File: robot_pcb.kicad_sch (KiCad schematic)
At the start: 112 parts, among them J1 Raspberry_Pi_2_3, J10 Servo_TrayRelease, J14 Motor FR, J16 19V Output, J17 Programmer, J2 Power_Bypass, J23 Motor BR, J25 ConductClaw, J26 Motor BL, J27 TOF_Front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

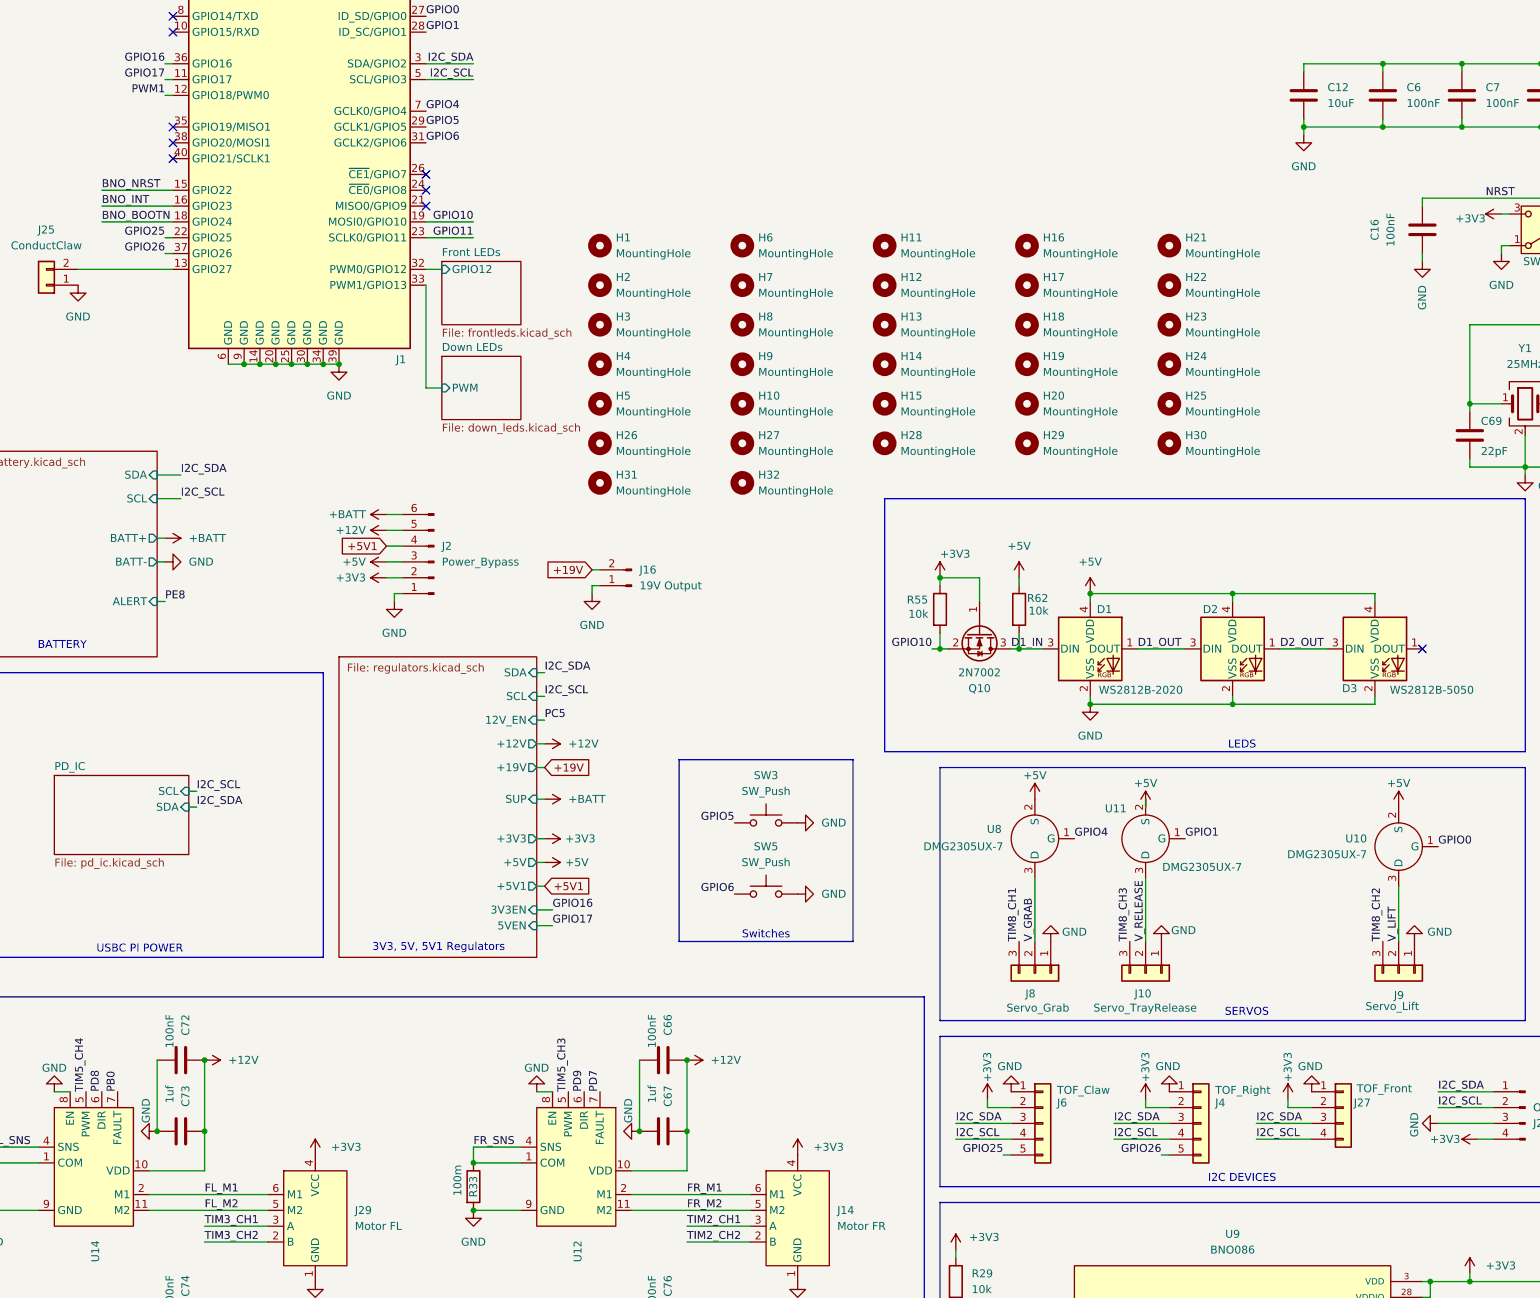
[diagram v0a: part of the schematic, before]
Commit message: 6 pin tof sensors
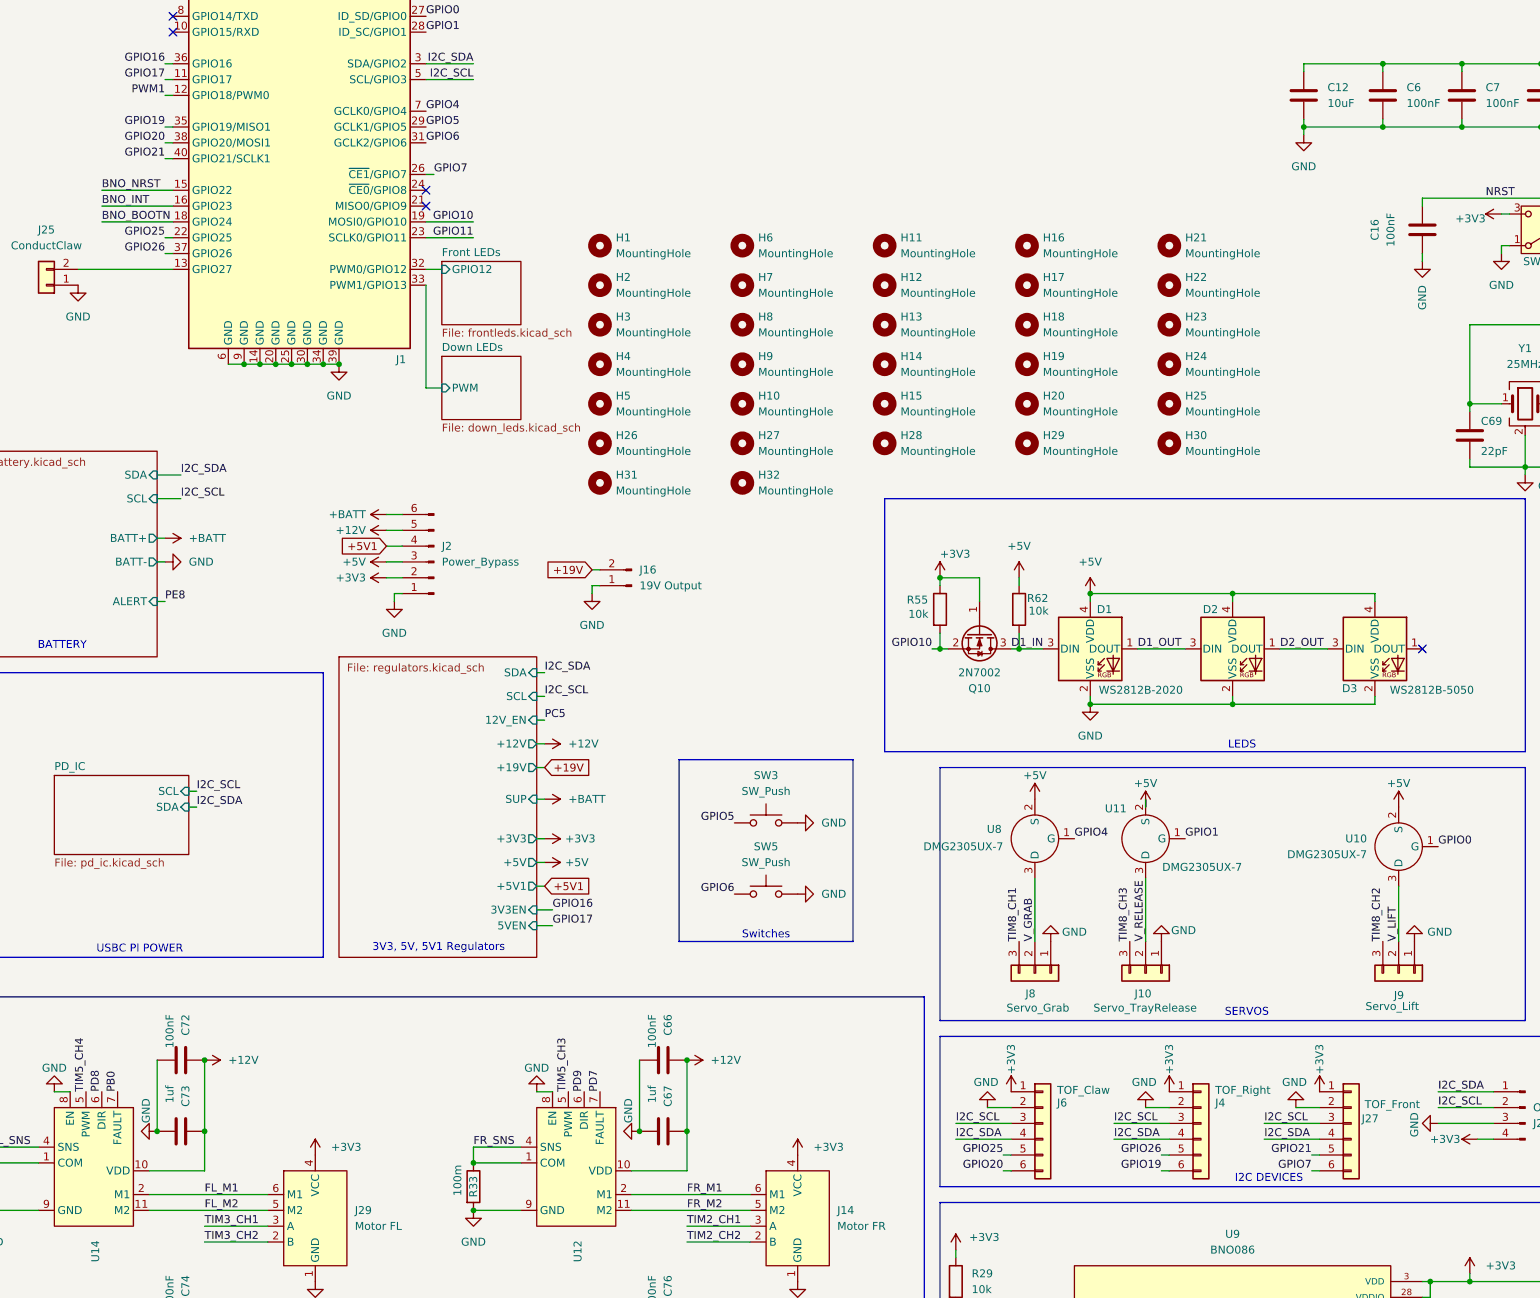
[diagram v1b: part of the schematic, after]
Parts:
- J10, J8, J9: LCSC (none) -> C158004
- J14, J23, J26, J29: LCSC (none) -> C157920
- J17, J7: LCSC (none) -> C52016392
- J25: LCSC (none) -> C5251182
- J27: footprint Connector_JST:JST_PH_B4B-PH-K_1x04_P2.00mm_Vertical -> Connector_JST:JST_PH_B6B-PH-K_1x06_P2.00mm_Vertical; symbol Connector_Generic:Conn_01x04 -> Connector_Generic:Conn_01x06
- J4, J6: footprint Connector_JST:JST_PH_B5B-PH-K_1x05_P2.00mm_Vertical -> Connector_JST:JST_PH_B6B-PH-K_1x06_P2.00mm_Vertical; symbol Connector_Generic:Conn_01x05 -> Connector_Generic:Conn_01x06
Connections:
- net +3V3: now also J27.1 (Pin_1), J4.1 (Pin_1), J6.1 (Pin_1); no longer J27.2 (Pin_2), J4.2 (Pin_2), J6.2 (Pin_2)
- net GND: now also J27.2 (Pin_2), J4.2 (Pin_2), J6.2 (Pin_2); no longer J27.1 (Pin_1), J4.1 (Pin_1), J6.1 (Pin_1)
- net I2C_SCL: now also J27.3 (Pin_3), J4.3 (Pin_3), J6.3 (Pin_3); no longer J27.4 (Pin_4), J4.4 (Pin_4), J6.4 (Pin_4)
- net I2C_SDA: now also J27.4 (Pin_4), J4.4 (Pin_4), J6.4 (Pin_4); no longer J27.3 (Pin_3), J4.3 (Pin_3), J6.3 (Pin_3)
- net GPIO7: now reaches J1.26 (~{CE1}/GPIO7)
- net GPIO7: now also J27.6 (Pin_6)
- net GPIO19: now reaches J1.35 (GPIO19/MISO1)
- net GPIO19: now also J4.6 (Pin_6)
- net GPIO20: now reaches J1.38 (GPIO20/MOSI1)
- net GPIO20: now also J6.6 (Pin_6)
- net GPIO21: now reaches J1.40 (GPIO21/SCLK1)
- net GPIO21: now also J27.5 (Pin_5)
- no-connect marks 66 -> 62

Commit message: yes
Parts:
- J16: LCSC (none) -> C158007
- J2: LCSC (none) -> C52016393
- J27, J4, J6: LCSC (none) -> C495261
- J28: LCSC (none) -> C2718488
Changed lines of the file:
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@@
 			)
 		)
-		(property "LCSC" ""
+		(property "LCSC" "C495261"
 			(at 237.49 208.28 0)
 			(effects
@@
 			)
 		)
+		(property "LCSC" "C495261"
+			(at 213.36 208.28 0)
+			(effects
+				(font
+					(size 1.27 1.27)
+				)
+				(hide yes)
+			)
+		)
 		(pin "3"
 		)
@@
 			)
 		)
-		(property "LCSC" ""
+		(property "LCSC" "C2718488"
 			(at 265.43 205.74 0)
 			(effects
@@
 			)
 		)
+		(property "LCSC" "C158007"
+			(at 121.92 121.92 0)
+			(effects
+				(font
+					(size 1.27 1.27)
+				)
+				(hide yes)
+			)
+		)
 		(pin "2"
 		)
@@
 			)
 		)
+		(property "LCSC" "C52016393"
+			(at 90.17 118.11 0)
+			(effects
+				(font
+					(size 1.27 1.27)
+				)
+				(hide yes)
+			)
+		)
 		(pin "5"
 		)
@@
 			(at 187.96 208.28 0)
 			(effects
+				(font
+					(size 1.27 1.27)
+				)
+				(hide yes)
+			)
+		)
+		(property "LCSC" "C495261"
+			(at 187.96 208.28 0)
+			(effects

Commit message: more lcsc
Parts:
- J1: LCSC (none) -> C50980
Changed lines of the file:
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@@
 			)
 		)
-		(property "LCSC" ""
+		(property "LCSC" "C50980"
 			(at 68.58 53.34 0)
 			(effects

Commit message: ALL LCSC PARTS DONE
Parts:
- M1: LCSC (none) -> C240840
- U12, U14, U15, U16: LCSC (none) -> C194048
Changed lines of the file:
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@@
 			)
 		)
+		(property "LCSC" "C194048"
+			(at 121.92 251.46 0)
+			(effects
+				(font
+					(size 1.27 1.27)
+				)
+				(hide yes)
+			)
+		)
 		(pin "11"
 		)
@@
 			)
 		)
+		(property "LCSC" "C240840"
+			(at 339.09 240.03 0)
+			(effects
+				(font
+					(size 1.27 1.27)
+				)
+				(hide yes)
+			)
+		)
 		(pin "3"
 		)
@@
 			)
 		)
+		(property "LCSC" "C194048"
+			(at 44.45 251.46 0)
+			(effects
+				(font
+					(size 1.27 1.27)
+				)
+				(hide yes)
+			)
+		)
 		(pin "11"
 		)
@@
 			)
 		)
+		(property "LCSC" "C194048"
+			(at 121.92 209.55 0)
+			(effects
+				(font
+					(size 1.27 1.27)
+				)
+				(hide yes)
+			)
+		)
 		(pin "11"
 		)
@@
 			(at 44.45 209.55 0)
 			(effects
+				(font
+					(size 1.27 1.27)
+				)
+				(hide yes)
+			)
+		)
+		(property "LCSC" "C194048"
+			(at 44.45 209.55 0)
+			(effects

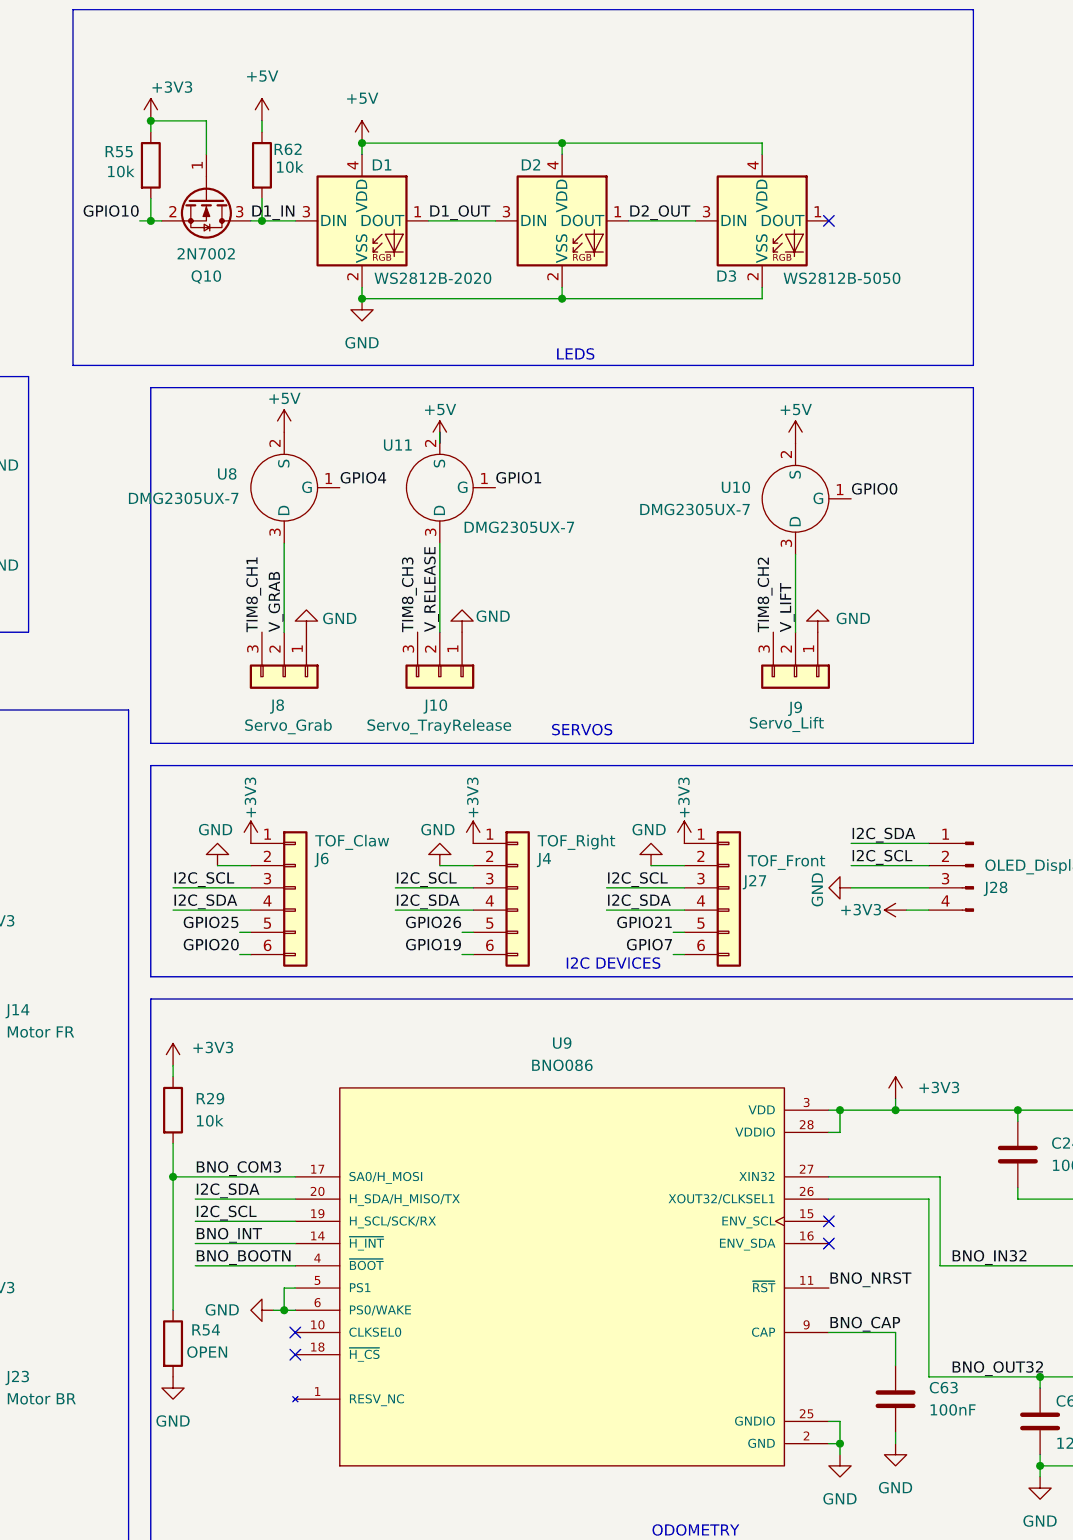
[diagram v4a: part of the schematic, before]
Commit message: Fixed errors with open resistors and led
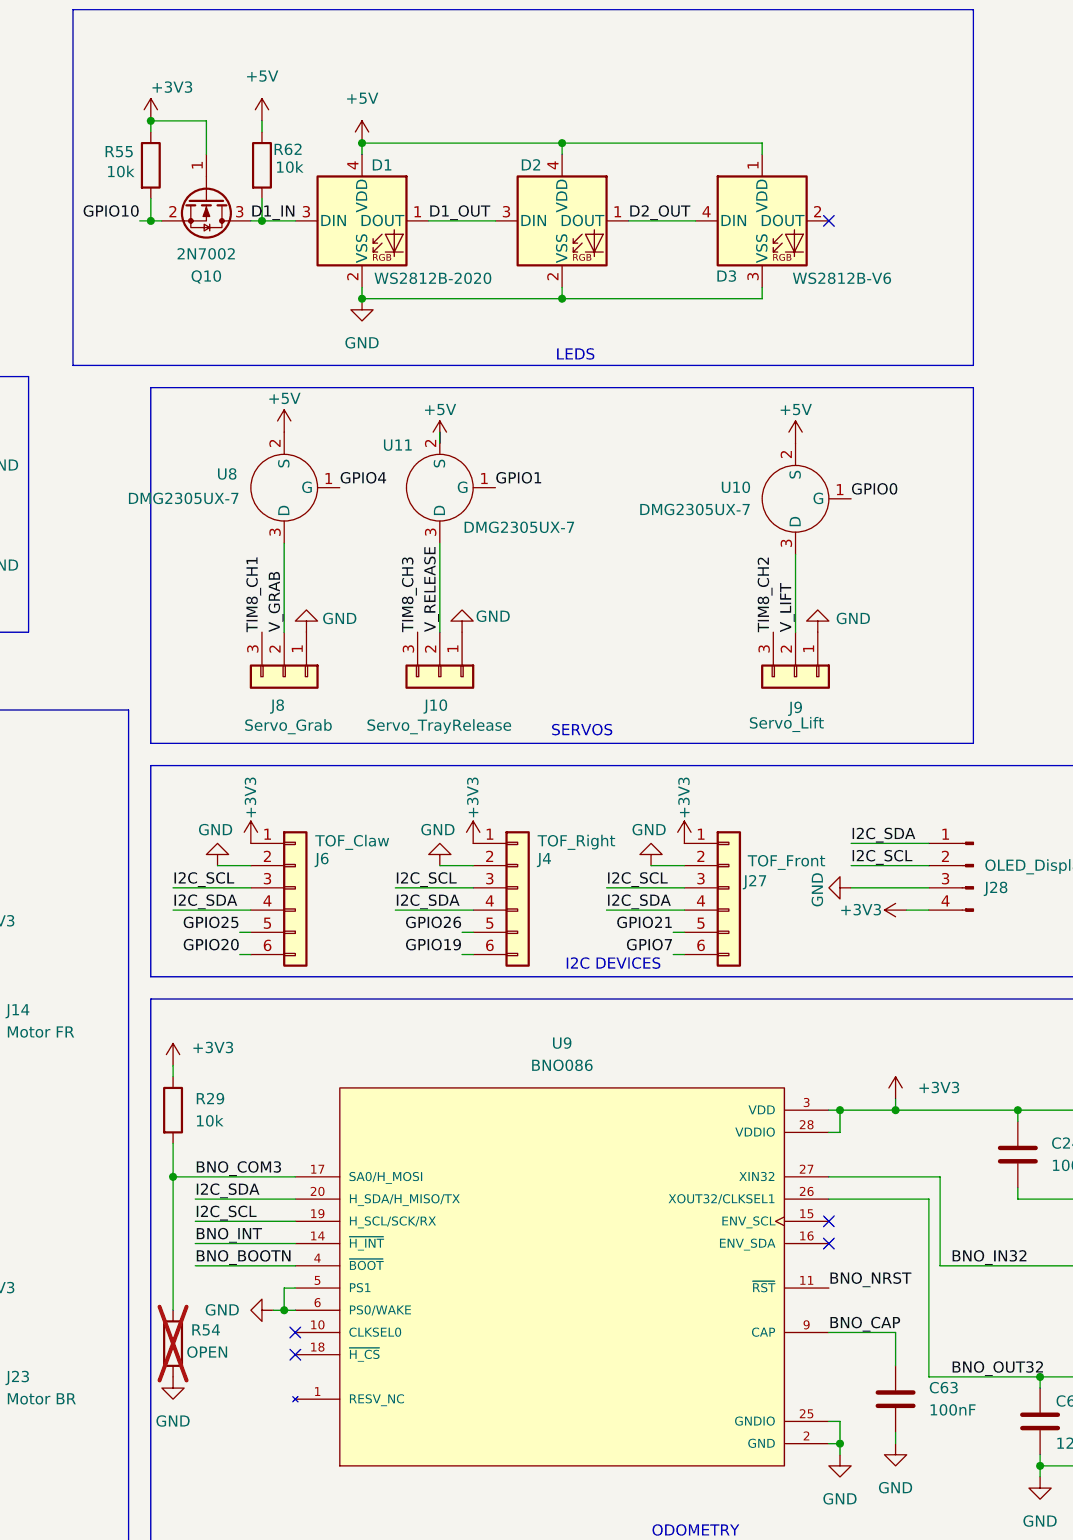
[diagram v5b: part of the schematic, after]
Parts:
- D3: value WS2812B-5050 -> WS2812B-V6; symbol LED:WS2812B-2020 -> Dry_Lettuce:WS2812B-5050; LCSC C114586 -> C52917433
- R54: now not fitted; now left out of the parts list
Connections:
- net +5V: now also D3.1 (VDD); no longer D3.4 (VDD)
- net D2_OUT: now also D3.4 (DIN); no longer D3.3 (DIN)
- net GND: now also D3.3 (VSS); no longer D3.2 (VSS)
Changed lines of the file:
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@@
 	)
 	(symbol
-		(lib_id "LED:WS2812B-2020")
+		(lib_id "Dry_Lettuce:WS2812B-5050")
 		(at 241.3 132.08 0)
 		(unit 1)
@@
 			)
 		)
-		(property "Value" "WS2812B-5050"
+		(property "Value" "WS2812B-V6"
 			(at 250.444 138.684 0)
 			(effects
@@
 			)
 		)
-		(property "Datasheet" "https://cdn-shop.adafruit.com/product-files/4684/4684_WS2812B-2020_V1.3_EN.pdf"
+		(property "Datasheet" "https://www.lcsc.com/datasheet/C52917433.pdf"
 			(at 243.84 141.605 0)
 			(effects
@@
 			)
 		)
-		(property "Description" "RGB LED with integrated controller, 2.0 x 2.0 mm, 12 mA"
-			(at 241.3 132.08 0)
-			(effects
-				(font
-					(size 1.27 1.27)
-				)
-				(hide yes)
-			)
-		)
-		(property "LCSC" "C114586"
+		(property "Description" "RGB LED with integrated controller, 5.0 x 5.0 mm, 12 mA"
+			(at 271.272 145.034 0)
+			(effects
+				(font
+					(size 1.27 1.27)
+				)
+				(hide yes)
+			)
+		)
+		(property "LCSC" "C52917433"
 			(at 241.3 132.08 0)
 			(effects
@@
 		(unit 1)
 		(exclude_from_sim no)
-		(in_bom yes)
-		(on_board yes)
-		(dnp no)
+		(in_bom no)
+		(on_board yes)
+		(dnp yes)
 		(property "Reference" "R54"
 			(at 176.022 258.826 0)

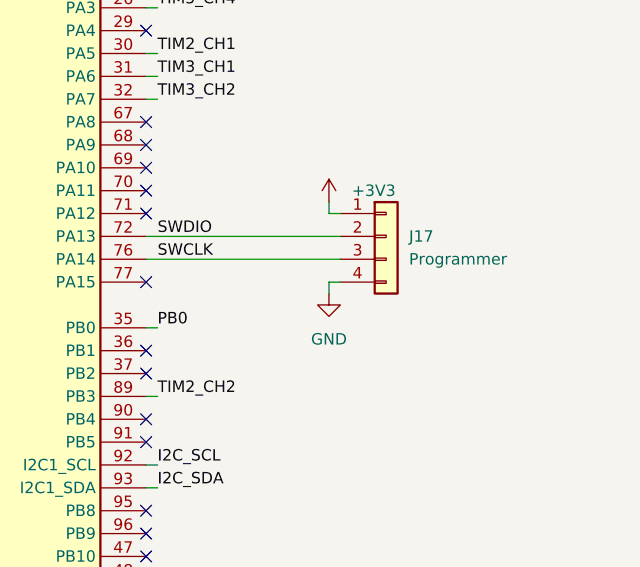
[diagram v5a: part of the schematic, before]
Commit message: added reset pin to stm32 debug output
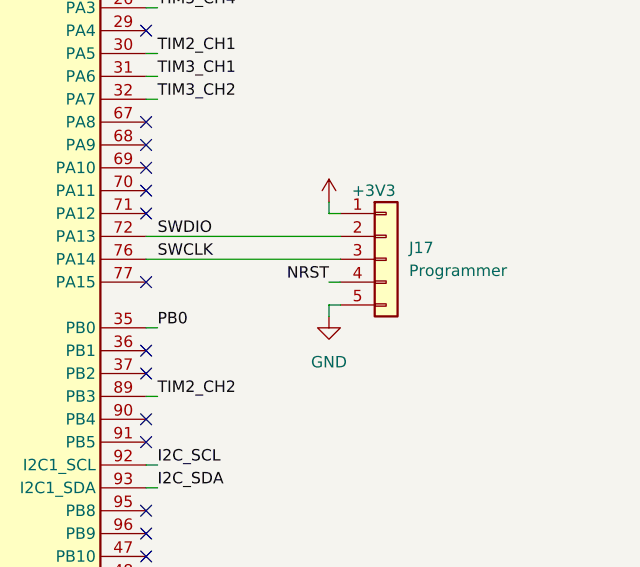
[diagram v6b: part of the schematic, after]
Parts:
- removed J17: Programmer, Connector_PinHeader_2.54mm:PinHeader_1x04_P2.54mm_Vertical, symbol Connector_Generic:Conn_01x04
- added J17: Programmer, Connector_PinHeader_2.54mm:PinHeader_1x05_P2.54mm_Vertical, symbol Connector_Generic:Conn_01x05
- U12, U14, U15, U16: value ~ -> (none)
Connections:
- net +3V3: now also J17.1 (Pin_1)
- net GND: now also J17.5 (Pin_5)
- net NRST: now also J17.4 (Pin_4)
- net SWCLK: now also J17.3 (Pin_3)
- net SWDIO: now also J17.2 (Pin_2)
